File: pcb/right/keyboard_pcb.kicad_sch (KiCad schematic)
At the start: 33 parts, among them J1 TRRS, K00 KEYSW, K01 KEYSW, K02 KEYSW, K03 KEYSW, K04 KEYSW, K05 KEYSW, K10 KEYSW, K11 KEYSW, K12 KEYSW, K13 KEYSW, K14 KEYSW, K15 KEYSW, K20 KEYSW, K21 KEYSW, K22 KEYSW, K23 KEYSW, K24 KEYSW, K25 KEYSW, K30 KEYSW, K31 KEYSW, K32 KEYSW, U2 Pico

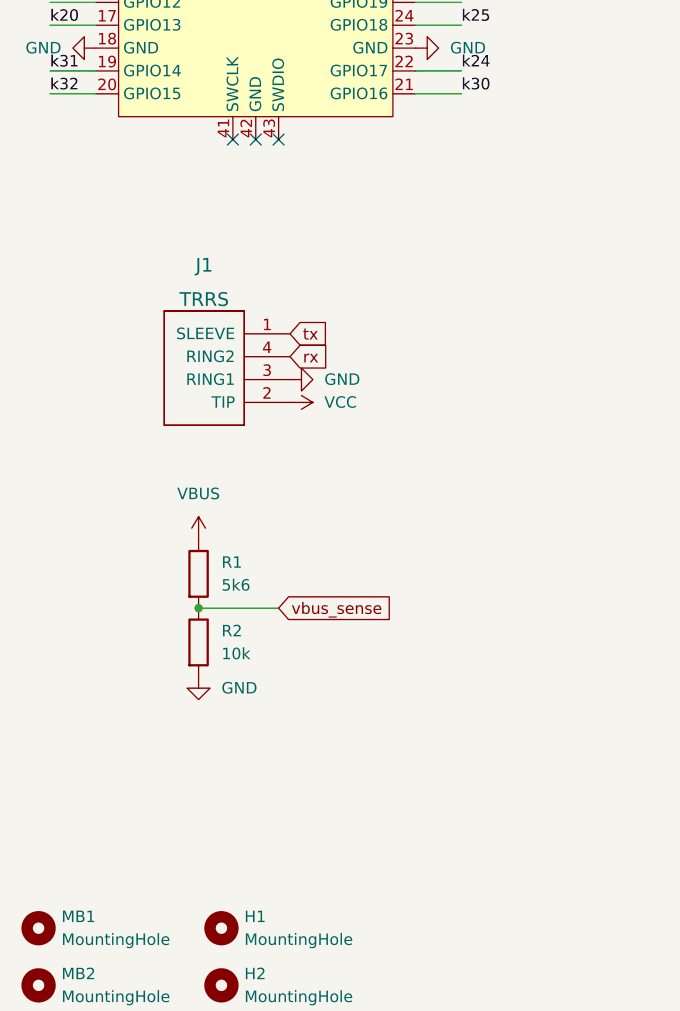
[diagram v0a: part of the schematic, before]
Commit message: Add right side, add fabrication outputs
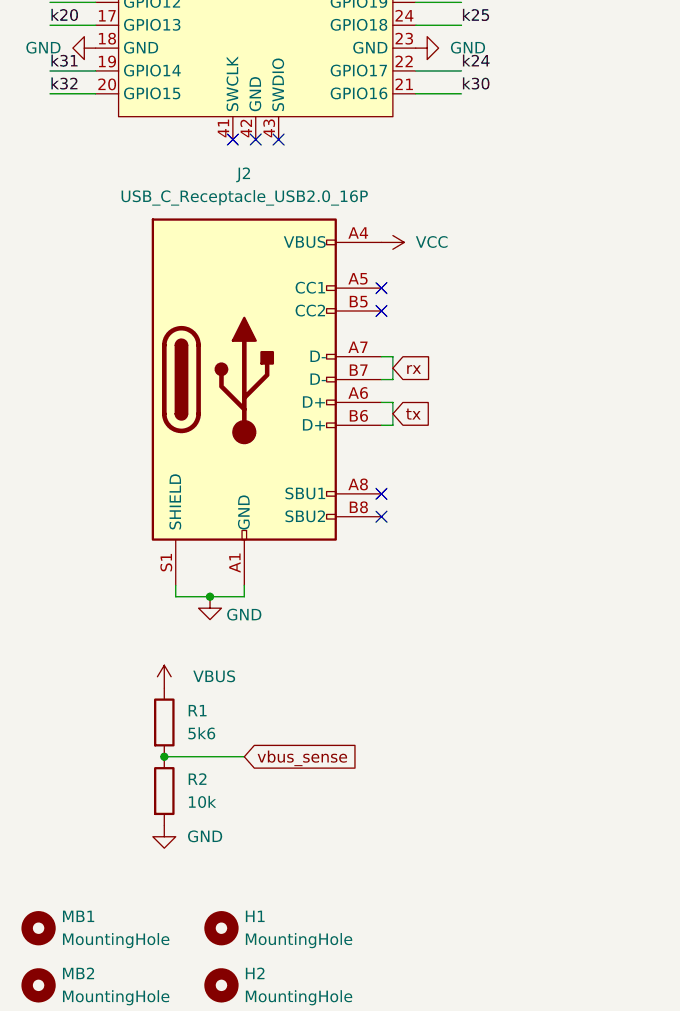
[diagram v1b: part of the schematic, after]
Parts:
- removed J1: TRRS, Resistor_SMD:R_1206_3216Metric_Pad1.30x1.75mm_HandSolder, symbol keebio:TRRS
- added J2: USB_C_Receptacle_USB2.0_16P, Connector_USB:USB_C_Receptacle_Palconn_UTC16-G, symbol Connector:USB_C_Receptacle_USB2.0_16P
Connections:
- net GND: now also J2.A1 (GND), J2.A12 (GND), J2.B1 (GND), J2.B12 (GND), J2.S1 (SHIELD)
- net VCC: now also J2.A4 (VBUS), J2.A9 (VBUS), J2.B4 (VBUS), J2.B9 (VBUS)
- net rx: now also J2.A7 (D-), J2.B7 (D-)
- net tx: now also J2.A6 (D+), J2.B6 (D+)
- no-connect marks 9 -> 13
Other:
- moved on the sheet: R1, R2

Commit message: Update right side
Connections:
- net rx: now also J2.A6 (D+), J2.B6 (D+); no longer J2.A7 (D-), J2.B7 (D-)
- net tx: now also J2.A7 (D-), J2.B7 (D-); no longer J2.A6 (D+), J2.B6 (D+)
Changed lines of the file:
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@@
 	(global_label "tx"
 		(shape input)
-		(at 66.04 113.03 0)
+		(at 66.04 107.95 0)
 		(fields_autoplaced yes)
 		(effects
@@
 		)
 		(property "Intersheetrefs" "${INTERSHEET_REFS}"
-			(at 70.2069 113.1094 0)
+			(at 70.2069 108.0294 0)
 			(effects
 				(font
@@
 	(global_label "rx"
 		(shape input)
-		(at 66.04 107.95 0)
+		(at 66.04 113.03 0)
 		(fields_autoplaced yes)
 		(effects
@@
 		)
 		(property "Intersheetrefs" "${INTERSHEET_REFS}"
-			(at 70.2674 108.0294 0)
+			(at 70.2674 113.1094 0)
 			(effects
 				(font
